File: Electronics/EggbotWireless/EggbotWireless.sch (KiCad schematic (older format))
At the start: 79 parts, among them J1 BATT, J2 Conn_01x03_Male, J3 USB_B_Micro, J4 AVR-ISP-6, J5 Conn_01x03_Female, J6 Conn_01x05_Male, M1 , M2 , M3 Motor_Servo, Q1 FDD8800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

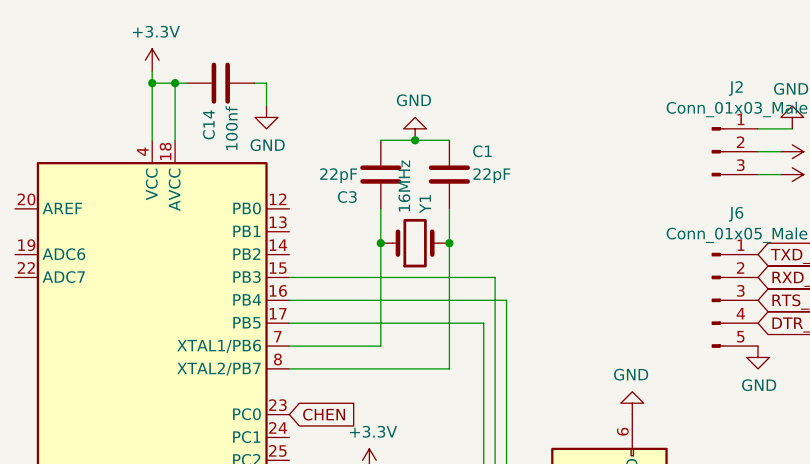
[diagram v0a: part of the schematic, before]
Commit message: [Board] fix some issues 1. change 5vboost output capacitor to 68 uF 2. change ATMega crystal to 12MHz
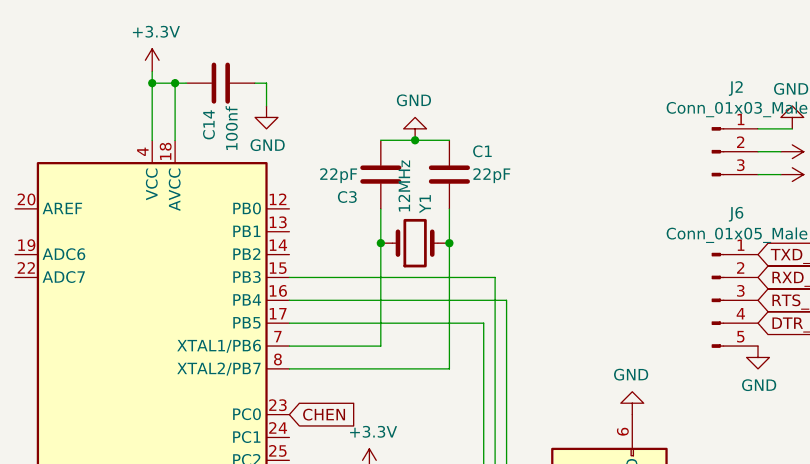
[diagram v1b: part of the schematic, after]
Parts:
- Y1: value 16MHz -> 12MHz
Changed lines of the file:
@@
 P 2700 1500
 F 0 "Y1" V 2746 1369 50  0000 R CNN
-F 1 "16MHz" V 2655 1369 50  0000 R CNN
+F 1 "12MHz" V 2655 1369 50  0000 R CNN
 F 2 "Crystal:Crystal_HC49-4H_Vertical" H 2700 1500 50  0001 C CNN
 F 3 "~" H 2700 1500 50  0001 C CNN

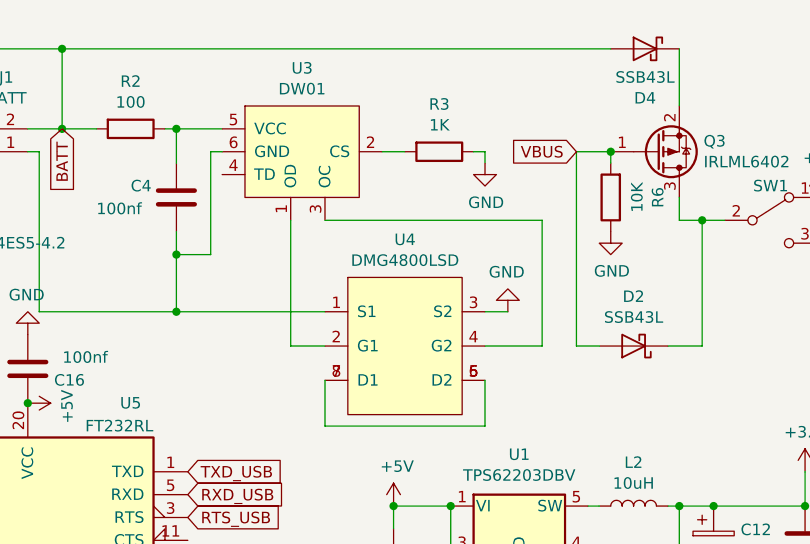
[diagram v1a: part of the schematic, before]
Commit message: change battery mosfet to FDS6898AZ Servo motor kind of works now, but not enough power for wi-fi, and it resets sometimes: 5v boost redesign needed - I didn't expect that much power draw from a servo motor
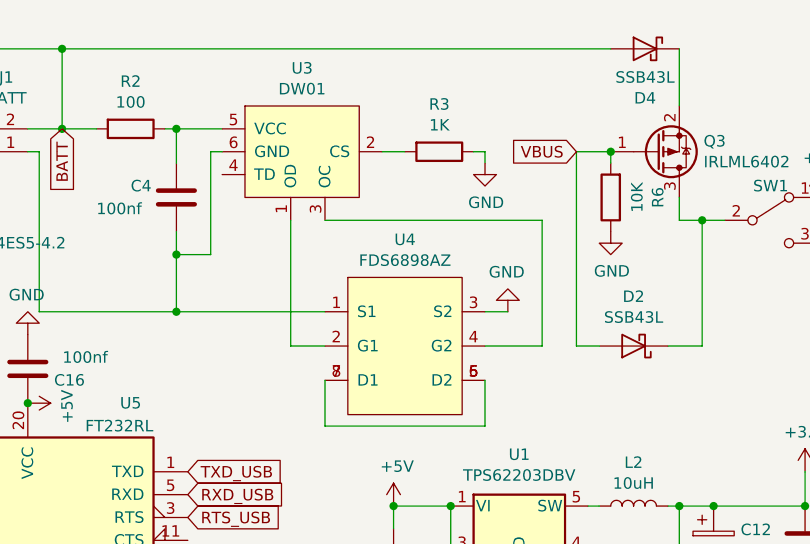
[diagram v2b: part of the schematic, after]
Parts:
- U4: value DMG4800LSD -> FDS6898AZ
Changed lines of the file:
@@
 P 9150 1600
 F 0 "U4" H 9150 1715 50  0000 C CNN
-F 1 "DMG4800LSD" H 9150 1624 50  0000 C CNN
+F 1 "FDS6898AZ" H 9150 1624 50  0000 C CNN
 F 2 "Package_SO:SO-8_3.9x4.9mm_P1.27mm" H 9040 1715 50  0001 C CNN
 F 3 "" H 9040 1715 50  0001 C CNN

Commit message: add 5v booster bypass for servo
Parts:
- added JP4: Jumper, Connector_PinHeader_2.54mm:PinHeader_1x02_P2.54mm_Vertical, symbol Device:Jumper
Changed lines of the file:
@@
 Text GLabel 3200 3600 0    50   Input ~ 0
 SERVOPWR
+$Comp
+L EggbotWireless-rescue:+5V-power #PWR0163
+U 1 1 5F040FF3
+P 2650 4350
+F 0 "#PWR0163" H 2650 4200 50  0001 C CNN
+F 1 "+5V" H 2665 4523 50  0000 C CNN
+F 2 "" H 2650 4350 50  0001 C CNN
+F 3 "" H 2650 4350 50  0001 C CNN
+	1    2650 4350
+	1    0    0    -1
+$EndComp
+$Comp
+L Device:Jumper JP4
+U 1 1 5F042E8B
+P 2950 4350
+F 0 "JP4" H 2950 4614 50  0000 C CNN
+F 1 "Jumper" H 2950 4523 50  0000 C CNN
+F 2 "Connector_PinHeader_2.54mm:PinHeader_1x02_P2.54mm_Vertical" H 2950 4350 50  0001 C CNN
+F 3 "~" H 2950 4350 50  0001 C CNN
+	1    2950 4350
+	1    0    0    -1
+$EndComp
+Text GLabel 3250 4350 3    50   Input ~ 0
+SERVOPWR
 $EndSCHEMATC

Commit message: delete 5v boost circuit
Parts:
- removed JP4: Jumper, Connector_PinHeader_2.54mm:PinHeader_1x02_P2.54mm_Vertical, symbol Device:Jumper
- added C18: 68uF, Capacitor_SMD:CP_Elec_4x5.8, symbol EggbotWireless-rescue:CP-Device
- added C19: 10uF, Capacitor_SMD:C_0805_2012Metric_Pad1.18x1.45mm_HandSolder, symbol EggbotWireless-rescue:C-Device
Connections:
- net labels removed: SERVOPWR
- wire segments 236 -> 245
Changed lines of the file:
@@
 $Descr A4 11693 8268
 encoding utf-8
-Sheet 1 2
+Sheet 1 1
 Title ""
 Date ""
@@
 Wire Wire Line
 	10050 650  7650 650
-Text GLabel 3200 3600 0    50   Input ~ 0
-SERVOPWR
-$Comp
-L EggbotWireless-rescue:+5V-power #PWR0163
-U 1 1 5F040FF3
-P 2650 4350
-F 0 "#PWR0163" H 2650 4200 50  0001 C CNN
-F 1 "+5V" H 2665 4523 50  0000 C CNN
-F 2 "" H 2650 4350 50  0001 C CNN
-F 3 "" H 2650 4350 50  0001 C CNN
-	1    2650 4350
-	1    0    0    -1
-$EndComp
-$Comp
-L Device:Jumper JP4
-U 1 1 5F042E8B
-P 2950 4350
-F 0 "JP4" H 2950 4614 50  0000 C CNN
-F 1 "Jumper" H 2950 4523 50  0000 C CNN
-F 2 "Connector_PinHeader_2.54mm:PinHeader_1x02_P2.54mm_Vertical" H 2950 4350 50  0001 C CNN
-F 3 "~" H 2950 4350 50  0001 C CNN
-	1    2950 4350
-	1    0    0    -1
-$EndComp
-Text GLabel 3250 4350 3    50   Input ~ 0
-SERVOPWR
-$Sheet
-S 5450 6600 1200 950
-U 5E1045DA
-F0 "5v Boost" 50
-F1 "5vBoost.sch" 50
-$EndSheet
+$Comp
+L EggbotWireless-rescue:+5V-power #PWR0109
+U 1 1 5FB1D7BE
+P 2500 4000
+F 0 "#PWR0109" H 2500 3850 50  0001 C CNN
+F 1 "+5V" H 2515 4173 50  0000 C CNN
+F 2 "" H 2500 4000 50  0001 C CNN
+F 3 "" H 2500 4000 50  0001 C CNN
+	1    2500 4000
+	0    -1   -1   0
+$EndComp
+$Comp
+L EggbotWireless-rescue:CP-Device C18
+U 1 1 5FB522B1
+P 2700 4150
+AR Path="/5FB522B1" Ref="C18"  Part="1"
+AR Path="/5E1045DA/5FB522B1" Ref="C?"  Part="1"
+AR Path="/5FB4B9D9/5FB522B1" Ref="C?"  Part="1"
+F 0 "C18" H 2818 4196 50  0000 L CNN
+F 1 "68uF" H 2818 4105 50  0000 L CNN
+F 2 "Capacitor_SMD:CP_Elec_4x5.8" H 2738 4000 50  0001 C CNN
+F 3 "~" H 2700 4150 50  0001 C CNN
+	1    2700 4150
+	1    0    0    -1
+$EndComp
+$Comp
+L EggbotWireless-rescue:C-Device C19
+U 1 1 5FB522B7
+P 3150 4150
+AR Path="/5FB522B7" Ref="C19"  Part="1"
+AR Path="/5E1045DA/5FB522B7" Ref="C?"  Part="1"
+AR Path="/5FB4B9D9/5FB522B7" Ref="C?"  Part="1"
+F 0 "C19" H 3265 4196 50  0000 L CNN
+F 1 "10uF" H 3265 4105 50  0000 L CNN
+F 2 "Capacitor_SMD:C_0805_2012Metric_Pad1.18x1.45mm_HandSolder" H 3188 4000 50  0001 C CNN
+F 3 "~" H 3150 4150 50  0001 C CNN
+	1    3150 4150
+	1    0    0    -1
+$EndComp
+Wire Wire Line
+	2500 4000 2700 4000
+Wire Wire Line
+	3150 4000 2850 4000
+Connection ~ 2700 4000
+Wire Wire Line
+	2850 4000 2850 3600
+Wire Wire Line
+	2850 3600 3200 3600
+Connection ~ 2850 4000
+Wire Wire Line
+	2850 4000 2700 4000
+$Comp
+L EggbotWireless-rescue:GND-power-Catfi-rescue #PWR0154
+U 1 1 5FB95FEE
+P 2900 4350
+F 0 "#PWR0154" H 2900 4100 50  0001 C CNN
+F 1 "GND" H 2905 4177 50  0000 C CNN
+F 2 "" H 2900 4350 50  0001 C CNN
+F 3 "" H 2900 4350 50  0001 C CNN
+	1    2900 4350
+	1    0    0    -1
+$EndComp
+Wire Wire Line
+	2900 4350 2700 4350
+Wire Wire Line
+	2700 4350 2700 4300
+Wire Wire Line
+	2900 4350 3150 4350
+Wire Wire Line
+	3150 4350 3150 4300
+Connection ~ 2900 4350
 $EndSCHEMATC

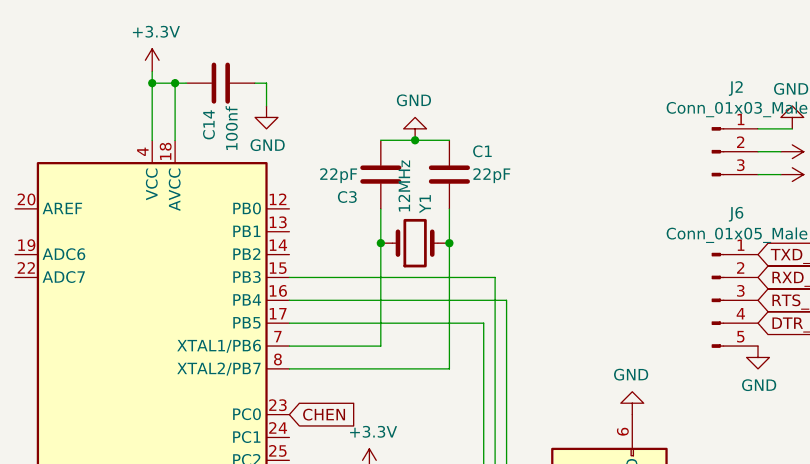
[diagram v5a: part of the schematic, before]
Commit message: change crystal to 16MHz
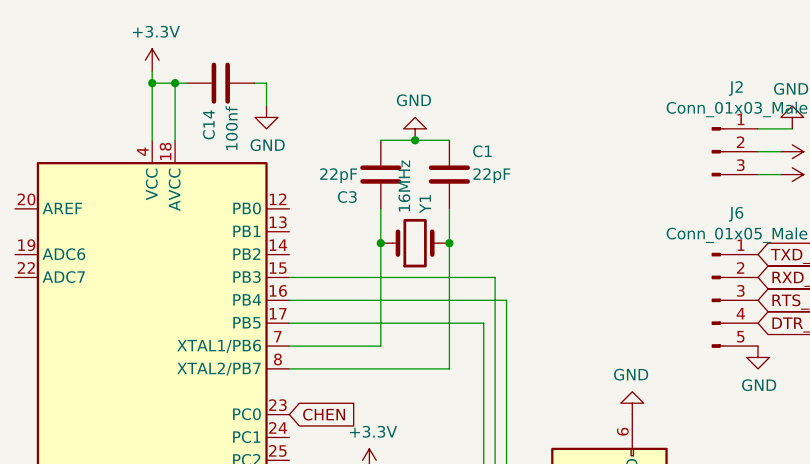
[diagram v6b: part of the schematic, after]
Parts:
- Y1: value 12MHz -> 16MHz
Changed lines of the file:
@@
 P 2700 1500
 F 0 "Y1" V 2746 1369 50  0000 R CNN
-F 1 "12MHz" V 2655 1369 50  0000 R CNN
+F 1 "16MHz" V 2655 1369 50  0000 R CNN
 F 2 "Crystal:Crystal_HC49-4H_Vertical" H 2700 1500 50  0001 C CNN
 F 3 "~" H 2700 1500 50  0001 C CNN

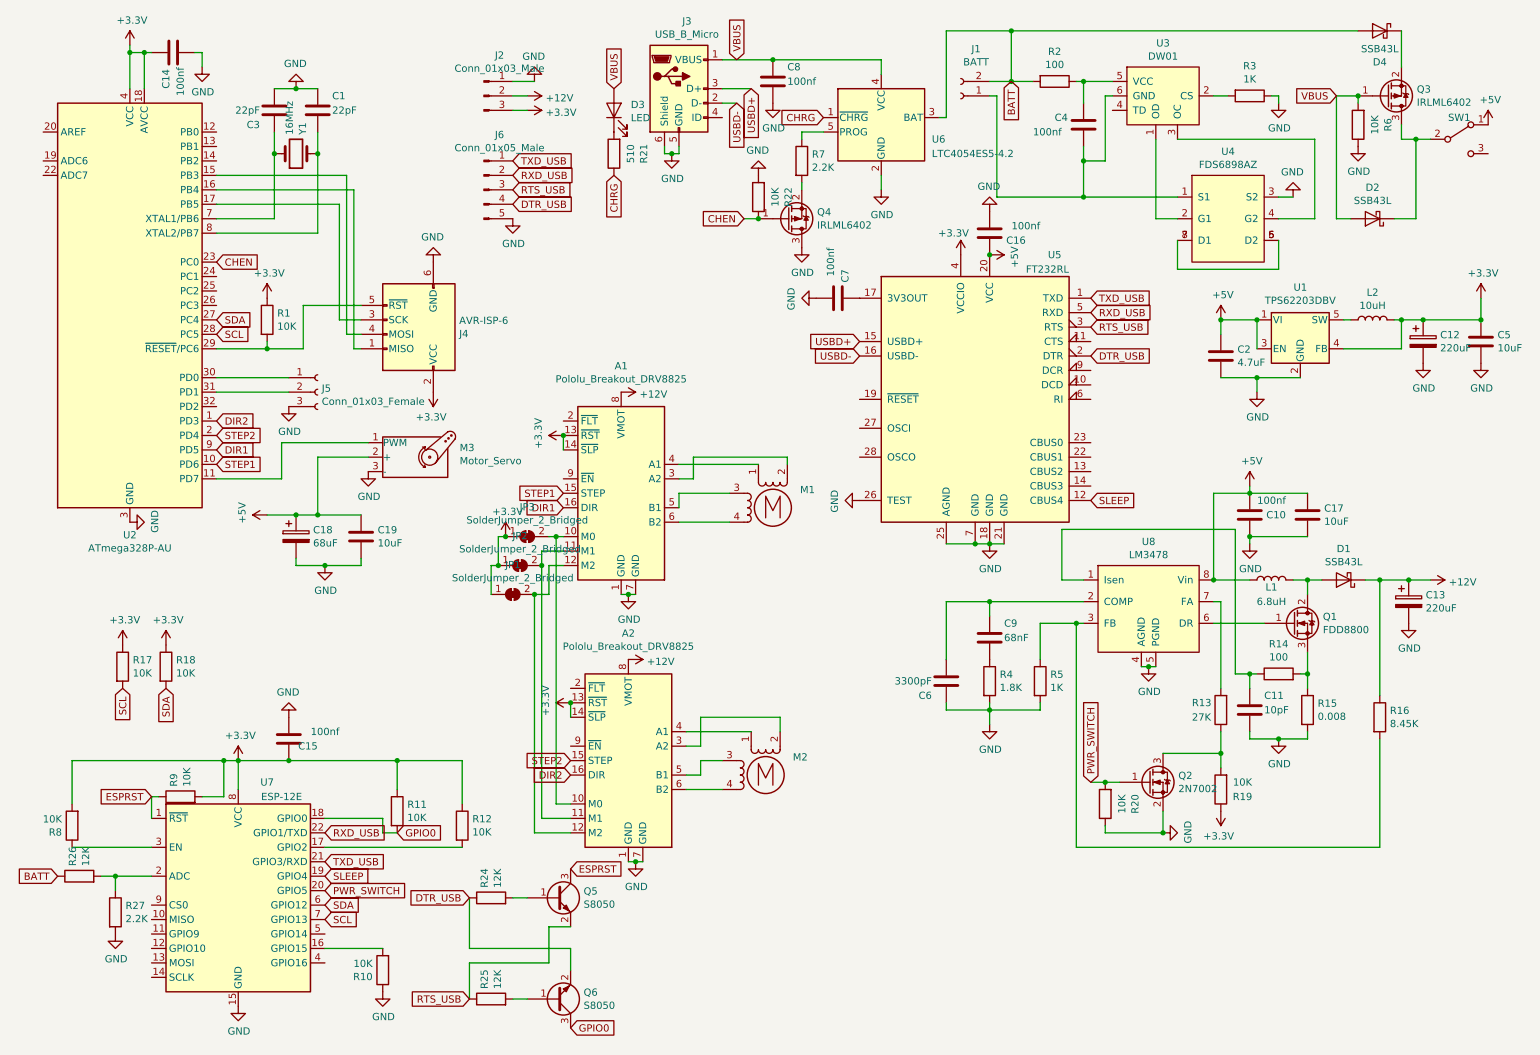
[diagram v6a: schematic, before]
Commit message: remove all remnants of battery circuitry. Hopefully works
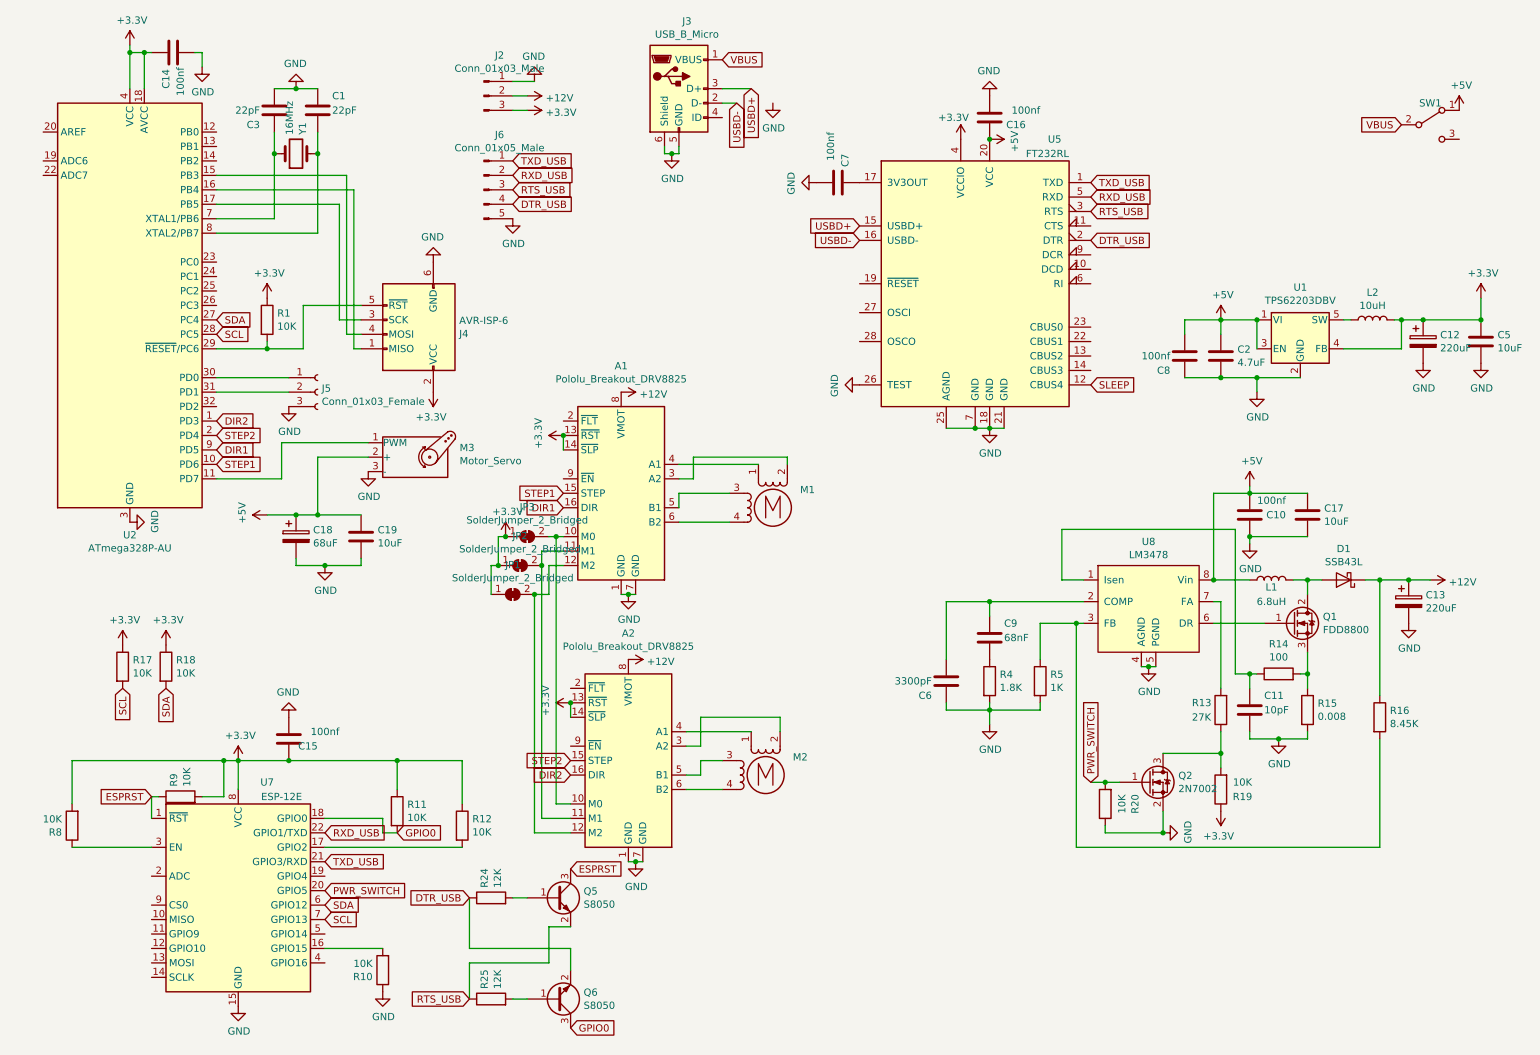
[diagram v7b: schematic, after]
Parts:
- removed C4: 100nf, Capacitor_SMD:C_0805_2012Metric_Pad1.15x1.40mm_HandSolder, symbol EggbotWireless-rescue:C-Device-Catfi-rescue
- removed D2, D4: SSB43L, Diode_SMD:D_SMB_Handsoldering, symbol EggbotWireless-rescue:D_Schottky-Device
- removed D3: LED, Diode_SMD:D_0805_2012Metric_Pad1.15x1.40mm_HandSolder, symbol EggbotWireless-rescue:LED-Device
- removed J1: BATT, Connector_PinHeader_2.54mm:PinHeader_1x02_P2.54mm_Vertical, symbol EggbotWireless-rescue:Conn_01x02_Female-Connector-Catfi-rescue
- removed Q3, Q4: IRLML6402, Package_TO_SOT_SMD:SOT-23, symbol EggbotWireless-rescue:IRLML6402-Transistor_FET
- removed R2: 100, Resistor_SMD:R_0805_2012Metric_Pad1.15x1.40mm_HandSolder, symbol EggbotWireless-rescue:R-Device-Catfi-rescue
- removed R21: 510, Resistor_SMD:R_0805_2012Metric_Pad1.15x1.40mm_HandSolder, symbol EggbotWireless-rescue:R-Device-Catfi-rescue
- removed R22, R6: 10K, Resistor_SMD:R_0805_2012Metric_Pad1.15x1.40mm_HandSolder, symbol EggbotWireless-rescue:R-Device-Catfi-rescue
- removed R26: 12K, Resistor_SMD:R_0805_2012Metric_Pad1.15x1.40mm_HandSolder, symbol EggbotWireless-rescue:R-Device-Catfi-rescue
- removed R27, R7: 2.2K, Resistor_SMD:R_0805_2012Metric_Pad1.15x1.40mm_HandSolder, symbol EggbotWireless-rescue:R-Device-Catfi-rescue
- removed R3: 1K, Resistor_SMD:R_0805_2012Metric_Pad1.15x1.40mm_HandSolder, symbol EggbotWireless-rescue:R-Device-Catfi-rescue
- removed U3: DW01, Package_TO_SOT_SMD:SOT-23-6_Handsoldering, symbol EggbotWireless-rescue:DW01-DW01-Catfi-rescue
- removed U4: FDS6898AZ, Package_SO:SO-8_3.9x4.9mm_P1.27mm, symbol DMG4800LSD:DMG4800LSD
- removed U6: LTC4054ES5-4.2, Package_TO_SOT_SMD:TSOT-23-5, symbol EggbotWireless-rescue:LTC4054ES5-4.2-Battery_Management-Catfi-rescue
- C8: footprint Capacitor_SMD:C_0805_2012Metric_Pad1.15x1.40mm_HandSolder -> Capacitor_SMD:C_0805_2012Metric_Pad1.18x1.45mm_HandSolder
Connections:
- net +5V: now also C8.1
- net GND: now also C8.2; no longer C8.1
- net SLEEP: no longer U7.19 (GPIO4)
- net VBUS: now also SW1.2 (B); no longer C8.2
- net CHEN: no longer names the net of U2.23 (PC0)
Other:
- moved on the sheet: C16, C7, C8, SW1, U5

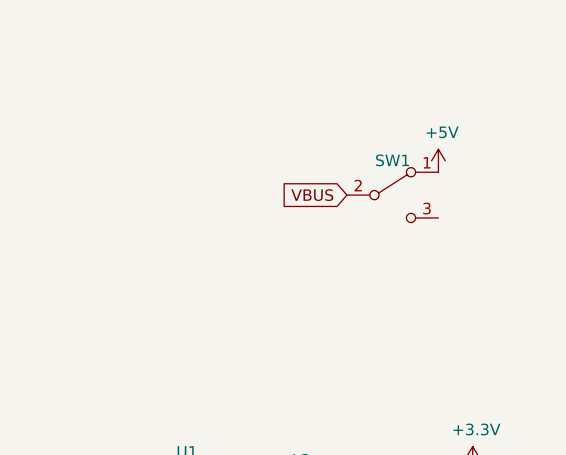
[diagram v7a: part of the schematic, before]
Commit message: remove power switch (no need without battery), v2.0!!!
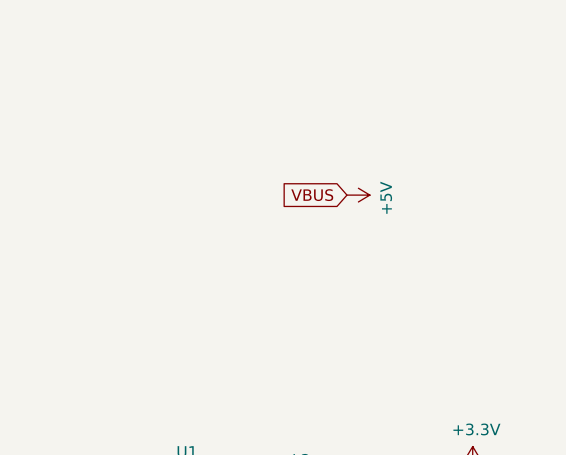
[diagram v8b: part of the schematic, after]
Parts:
- removed SW1: (no value), Button_Switch_THT:SW_CuK_OS102011MA1QN1_SPDT_Angled, symbol EggbotWireless-rescue:SW_SPDT-Switch
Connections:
- net VBUS is gone; now on net +5V: J3.1 (VBUS)
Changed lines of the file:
@@
 L EggbotWireless-rescue:+5V-power #PWR0130
 U 1 1 5D7ABED4
-P 10750 1200
-F 0 "#PWR0130" H 10750 1050 50  0001 C CNN
-F 1 "+5V" H 10765 1373 50  0000 C CNN
-F 2 "" H 10750 1200 50  0001 C CNN
-F 3 "" H 10750 1200 50  0001 C CNN
-	1    10750 1200
-	1    0    0    -1
-$EndComp
-$Comp
-L EggbotWireless-rescue:SW_SPDT-Switch SW1
-U 1 1 5CEB7C0D
-P 10550 1300
-F 0 "SW1" H 10550 1450 50  0000 C CNN
-F 1 " " H 10550 1494 50  0000 C CNN
-F 2 "Button_Switch_THT:SW_CuK_OS102011MA1QN1_SPDT_Angled" H 10550 1300 50  0001 C CNN
-F 3 "~" H 10550 1300 50  0001 C CNN
-	1    10550 1300
-	1    0    0    -1
+P 10350 1300
+F 0 "#PWR0130" H 10350 1150 50  0001 C CNN
+F 1 "+5V" H 10365 1473 50  0000 C CNN
+F 2 "" H 10350 1300 50  0001 C CNN
+F 3 "" H 10350 1300 50  0001 C CNN
+	1    10350 1300
+	0    1    1    0
 $EndComp
 Text GLabel 10350 1300 0    50   Input ~ 0
